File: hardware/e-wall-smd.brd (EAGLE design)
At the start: 50.8 x 48.3 mm, 74 parts, among them IC1 74HCT595D, IC2 74HCT595D, IC3 74HCT595D, IC4 74HCT595D, Q1 SI2302CDS, Q10 SI2302CDS, Q11 SI2302CDS, Q12 SI2302CDS, Q13 SI2302CDS, Q14 SI2302CDS, Q15 SI2302CDS, Q16 SI2302CDS, Q17 SI2302CDS, Q18 SI2302CDS, Q19 SI2302CDS, Q2 SI2302CDS, Q20 SI2302CDS, Q21 SI2302CDS, Q22 SI2302CDS, Q23 SI2302CDS, Q24 SI2302CDS, Q25 SI4214DDY, Q26 SI4214DDY, Q27 SI4214DDY, Q28 SI4214DDY, Q29 SI2302CDS, Q3 SI2302CDS, Q30 SI2302CDS, Q31 SI2347DS, Q4 SI2302CDS, Q5 SI2302CDS, Q6 SI2302CDS, Q7 SI2302CDS, Q8 SI2302CDS, Q9 SI2302CDS

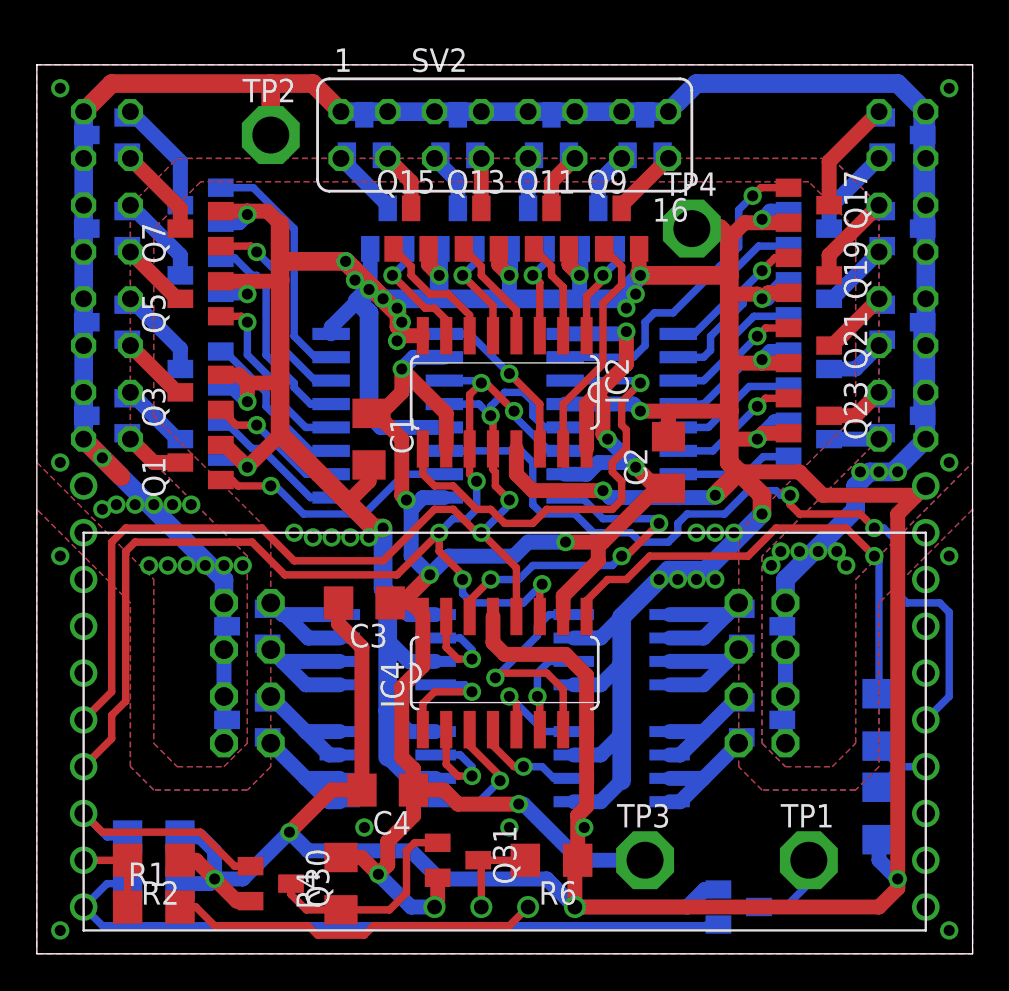
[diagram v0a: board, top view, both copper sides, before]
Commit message: moved some tracers to avoid layer change of high current paths
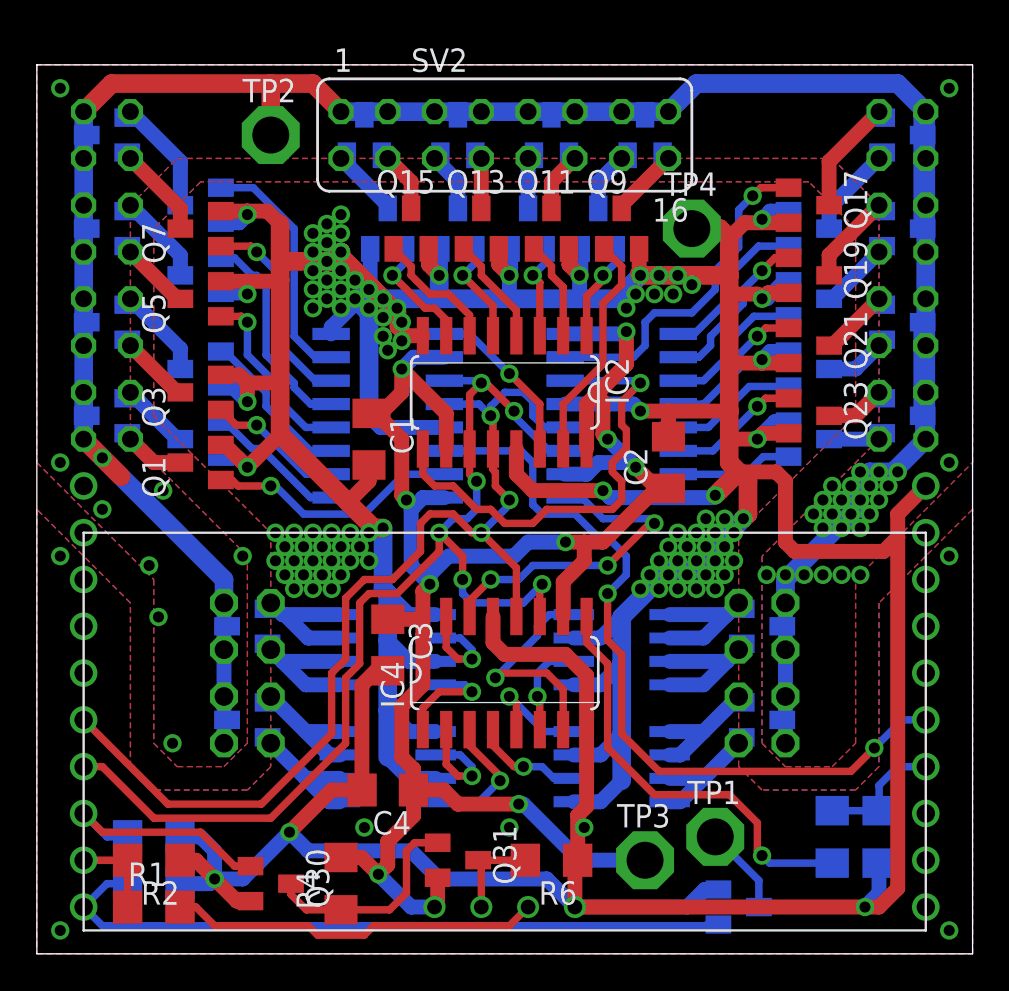
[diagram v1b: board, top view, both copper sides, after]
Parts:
- moved R8 6.84 mm to (43.2, 6.35), turned to 270 degrees
- moved TP1 5.24 mm to (36.8, 6.35)
- moved C3 2.62 mm to (19.1, 16.8), turned to 270 degrees
- moved R9 1.27 mm to (45.7, 6.35)
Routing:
- net SOMI: track 26.3 -> 23.3 mm
- net SOMI_UC: track 4.58 -> 6.87 mm
- net EN: track 54.7 -> 56.8 mm
- net GND: track 358.9 -> 357.3 mm, vias 48 -> 110
- net SIMO: track 43.3 -> 42.5 mm
- net SIG16: track 17.9 -> 18.5 mm
- net N$3: track 18.6 -> 18.1 mm
- net +12V: vias 26 -> 35

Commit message: Separate polygons for signal and power ground
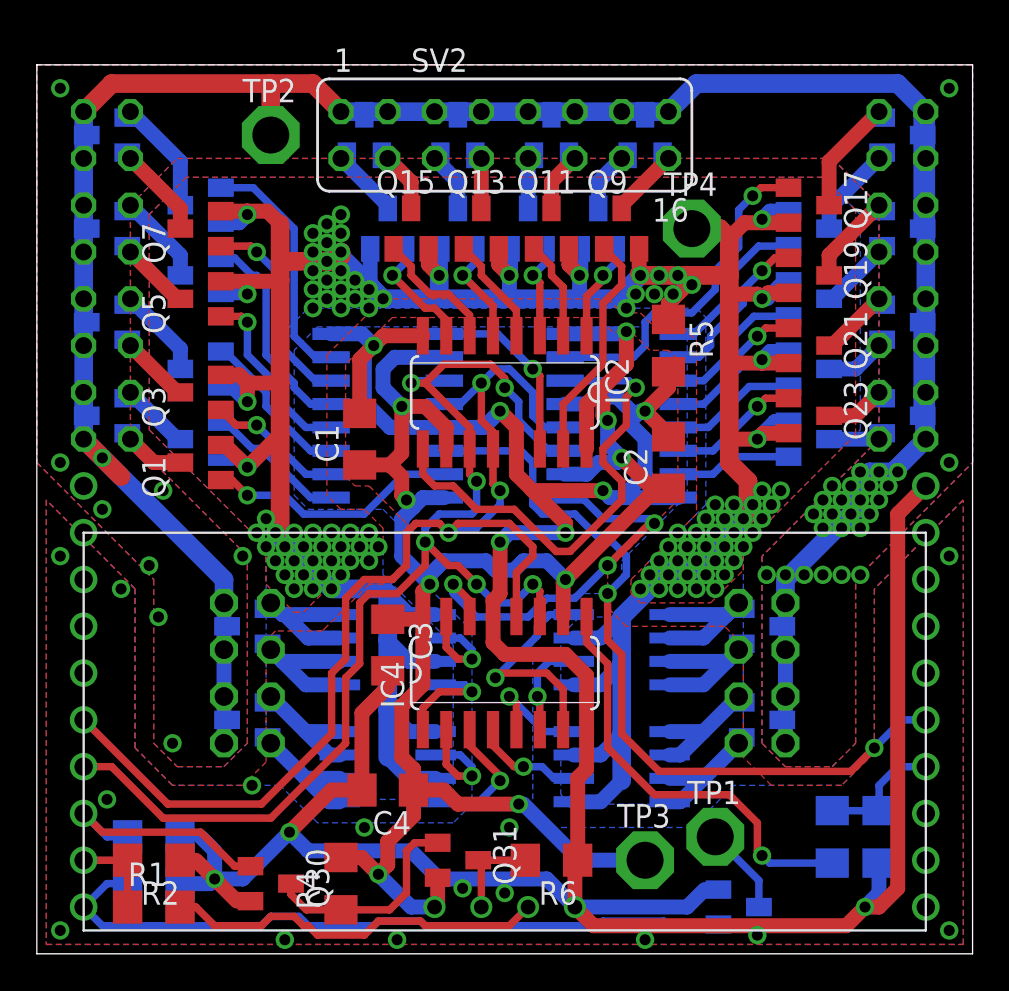
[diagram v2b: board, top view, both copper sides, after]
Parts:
- added R5: 0, resistor:R1206
- moved C1 0.51 mm to (17.5, 27.9), turned to 90 degrees
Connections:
- new net PWR_GND: Q1.2, Q10.2, Q11.2, Q12.2, Q13.2, Q14.2, Q15.2, Q16.2, Q17.2, Q18.2, Q19.2, Q2.2, Q20.2, Q21.2, Q22.2, Q23.2, Q24.2, Q25.1, Q25.3, Q26.1, Q26.3, Q27.1, Q27.3, Q28.1, Q28.3, Q3.2, Q4.2, Q5.2, Q6.2, Q7.2, Q8.2, Q9.2, R5.1, TP4.TP
- net GND: now also R5.2; no longer Q1.2, Q10.2, Q11.2, Q12.2, Q13.2, Q14.2, Q15.2, Q16.2, Q17.2, Q18.2, Q19.2, Q2.2, Q20.2, Q21.2, Q22.2, Q23.2, Q24.2, Q25.1, Q25.3, Q26.1, Q26.3, Q27.1, Q27.3, Q28.1, Q28.3, Q3.2, Q4.2, Q5.2, Q6.2, Q7.2, Q8.2, Q9.2, TP4.TP
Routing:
- net PWR_GND: track 0.00 -> 184.1 mm, vias 0 -> 103
- net GND: track 357.3 -> 173.6 mm, vias 110 -> 24
- net EN: track 56.8 -> 62.5 mm
- net CLK: track 60.2 -> 65.7 mm
- net N$3: track 18.1 -> 21.6 mm
- net N$2: track 25.3 -> 26.3 mm
- net N$1: track 9.20 -> 10.1 mm
- net N$37: track 37.8 -> 38.7 mm
- net +5V: track 106.4 -> 105.8 mm
- net ECHO: track 20.2 -> 20.8 mm
- added copper zone on layer 1, net PWR_GND
- added copper zone on layer 16, net PWR_GND

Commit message: Polygons for adding copper wire to increase maximal current
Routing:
- net PWR_GND: track 184.1 -> 184.5 mm, vias 103 -> 115
- net GND: vias 24 -> 31

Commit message: OSHW Logo
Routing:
- net +5V: track 105.8 -> 108.3 mm
- net GND: track 173.6 -> 171.9 mm
- net N$3: track 21.6 -> 22.7 mm
- net SIMO: track 42.5 -> 41.5 mm
- net N$2: track 26.3 -> 25.4 mm
- net PWR_GND: vias 115 -> 121
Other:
- board text added: "/home/daniw/Downloads/oshw-logo-800-px.bmp"
